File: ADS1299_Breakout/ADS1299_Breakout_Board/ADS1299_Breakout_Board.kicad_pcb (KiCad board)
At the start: 2 copper layers, 41 parts, among them J1 Conn_01x08_Pin, J2 Conn_01x08_Pin, J3 Conn_01x08_Pin, J4 Conn_01x08_Pin, J5 Conn_01x08_Pin, U1 TPD4E1B06DRLR, U2 ADS1299IPAG, U3 TPD4E1B06DRLR, U4 TPD4E1B06DRLR, U5 TPD4E1B06DRLR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

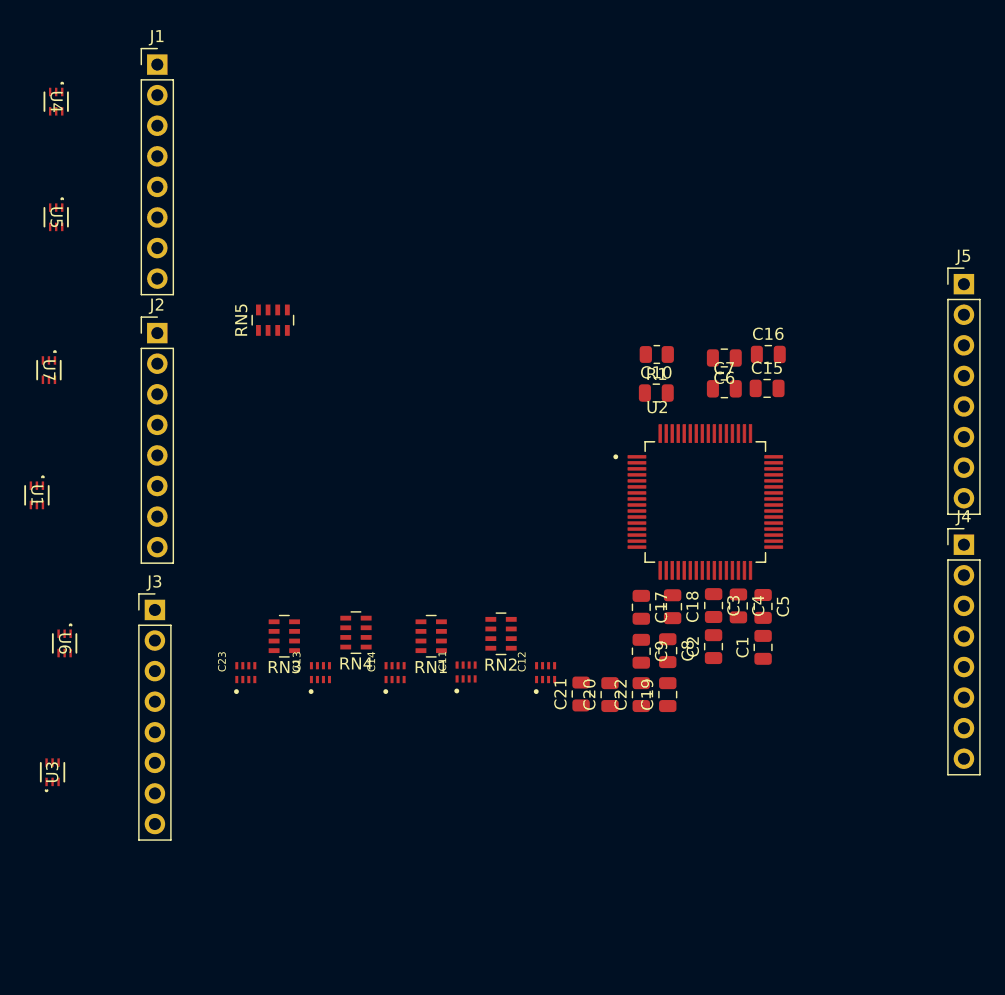
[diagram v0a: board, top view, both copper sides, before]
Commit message: Finished up traces
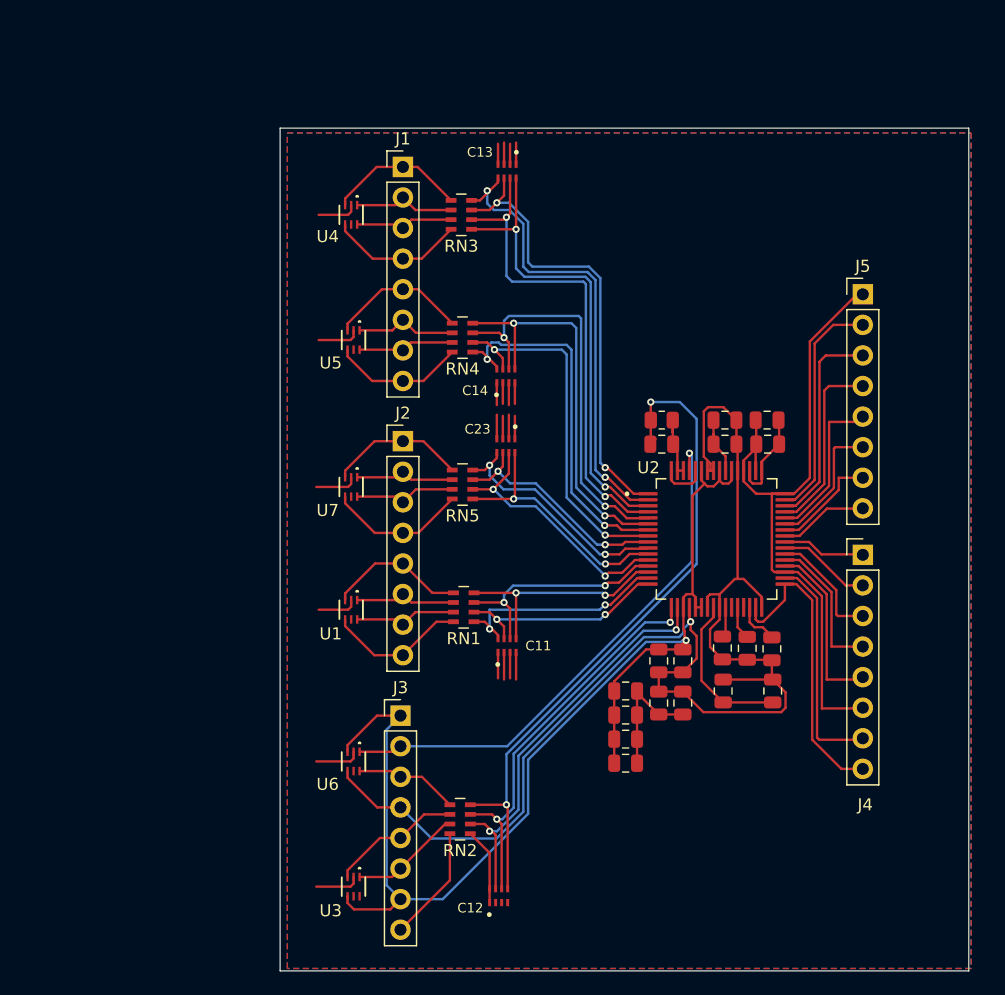
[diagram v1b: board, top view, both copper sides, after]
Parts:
- moved C13 44.4 mm to (147.7, 48.6), turned to -90 degrees
- moved RN3 38.0 mm to (143.8, 52.2)
- moved C23 28.7 mm to (147.6, 71.4), turned to -90 degrees
- moved U1 27.8 mm to (134.7, 85.0)
- moved U7 26.9 mm to (134.7, 74.8)
- moved U3 26.7 mm to (134.9, 108.0), turned to -90 degrees
- moved U5 26.7 mm to (134.9, 62.6)
- moved C14 26.3 mm to (147.6, 65.6)
- moved U4 26.2 mm to (134.7, 52.2)
- moved RN4 26.0 mm to (143.9, 62.4)
- moved U6 25.9 mm to (134.9, 97.6)
- moved J2 22.3 mm to (139.0, 71.0)
- moved J3 22.2 mm to (138.8, 93.8)
- moved J1 22.1 mm to (139.0, 48.2)
- moved RN5 20.8 mm to (143.9, 74.6), turned to 180 degrees
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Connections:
- C11 pad 5: /IN3N -> /IN2P
- C11 pad 6: /IN3P -> /IN2N
- C11 pad 7: /IN2N -> /IN1P
- C11 pad 8: /IN2P -> /IN1N
- C12 pad 5: /IN1N -> /BIAS_DRV
- C12 pad 6: /IN1P -> /_SRB1
- C12 pad 8: /_SRB1 -> AGND
- C13 pad 5: /BIAS_DRV -> /IN8P
- C13 pad 6: AGND -> /IN8N
- C13 pad 7: /IN8N -> /IN7P
- C13 pad 8: /IN8P -> /IN7N
- C14 pad 5: /IN7N -> /IN6P
- C14 pad 6: /IN7P -> /IN6N
- C14 pad 7: /IN6N -> /IN5P
- C14 pad 8: /IN6P -> /IN5N
- C23 pad 5: /IN5N -> /IN4P
- C23 pad 6: /IN5P -> /IN4N
- C23 pad 7: /IN4N -> /IN3P
- C23 pad 8: /IN4P -> /IN3N
- RN1 pad 1: /IN2P -> /IN1N
- RN1 pad 2: /IN2N -> /IN1P
- RN1 pad 3: /IN3P -> /IN2N
- RN1 pad 4: /IN3N -> /IN2P
- RN1 pad 5: /3N -> /2P
- RN1 pad 6: /3P -> /2N
- RN1 pad 7: /2N -> /1P
- RN1 pad 8: /2P -> /1N
- RN2 pad 1: /_SRB1 -> AGND
- RN2 pad 3: /IN1P -> /_SRB1
- RN2 pad 4: /IN1N -> /BIAS_DRV
- RN2 pad 5: /1N -> /BIAS
- RN2 pad 6: /1P -> /SRB1
- RN2 pad 8: /SRB1 -> AGND
- RN3 pad 1: /IN8P -> /IN7N
- RN3 pad 2: /IN8N -> /IN7P
- RN3 pad 3: AGND -> /IN8N
- RN3 pad 4: /BIAS_DRV -> /IN8P
- RN3 pad 5: /BIAS -> /8P
- RN3 pad 6: AGND -> /8N
- RN3 pad 7: /8N -> /7P
- RN3 pad 8: /8P -> /7N
- RN4 pad 1: /IN6P -> /IN5N
- RN4 pad 2: /IN6N -> /IN5P
- RN4 pad 3: /IN7P -> /IN6N
- RN4 pad 4: /IN7N -> /IN6P
- RN4 pad 5: /7N -> /6P
- RN4 pad 6: /7P -> /6N
- RN4 pad 7: /6N -> /5P
- RN4 pad 8: /6P -> /5N
- RN5 pad 1: /IN4P -> /IN3N
- RN5 pad 2: /IN4N -> /IN3P
- RN5 pad 3: /IN5P -> /IN4N
- RN5 pad 4: /IN5N -> /IN4P
- RN5 pad 5: /5N -> /4P
- RN5 pad 6: /5P -> /4N
- RN5 pad 7: /4N -> /3P
- RN5 pad 8: /4P -> /3N
- U3 pad 1: /SRB1 -> /SRB2
- U3 pad 3: /SRB2 -> /SRB1
- U3 pad 4: unconnected-(U3-IO3-Pad4) -> /AVDD
- U6 pad 1: /AVDD -> /BIASINV
- U6 pad 3: AGND -> /AVDD
- U6 pad 4: /BIAS -> /AVSS
- U6 pad 6: /AVSS -> /BIAS
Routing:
- net AGND: track 0.00 -> 123.2 mm
- net /AVSS: track 0.00 -> 111.1 mm, vias 0 -> 1
- net /AVDD: track 0.00 -> 98.8 mm, vias 0 -> 1
- net /BIAS_DRV: track 0.00 -> 57.4 mm, vias 0 -> 2
- net /DVDD: track 0.00 -> 56.4 mm
- net /BIASINV: track 0.00 -> 44.7 mm, vias 0 -> 1
- net /IN7P: track 0.00 -> 40.6 mm, vias 0 -> 2
- net /IN7N: track 0.00 -> 39.6 mm, vias 0 -> 2
- net /IN8P: track 0.00 -> 39.2 mm, vias 0 -> 2
- net /IN8N: track 0.00 -> 38.2 mm, vias 0 -> 2
- net /IN6N: track 0.00 -> 34.1 mm, vias 0 -> 2
- net /_SRB2: track 0.00 -> 34.0 mm, vias 0 -> 2
- net /_SRB1: track 0.00 -> 33.4 mm, vias 0 -> 2
- net /IN6P: track 0.00 -> 33.1 mm, vias 0 -> 2
- net /IN5N: track 0.00 -> 30.8 mm, vias 0 -> 2
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- added copper zone on B.Cu, net AGND
- added copper zone on F.Cu, net AGND
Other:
- board outline added: 57.2 x 70 mm
